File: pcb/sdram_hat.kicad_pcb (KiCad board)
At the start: 2 copper layers, 25 parts, among them J1 CONN_02X20, J2 CONN_02X20, J3 CONN_02X20, J4 CONN_02X20, J5 JACK_2P

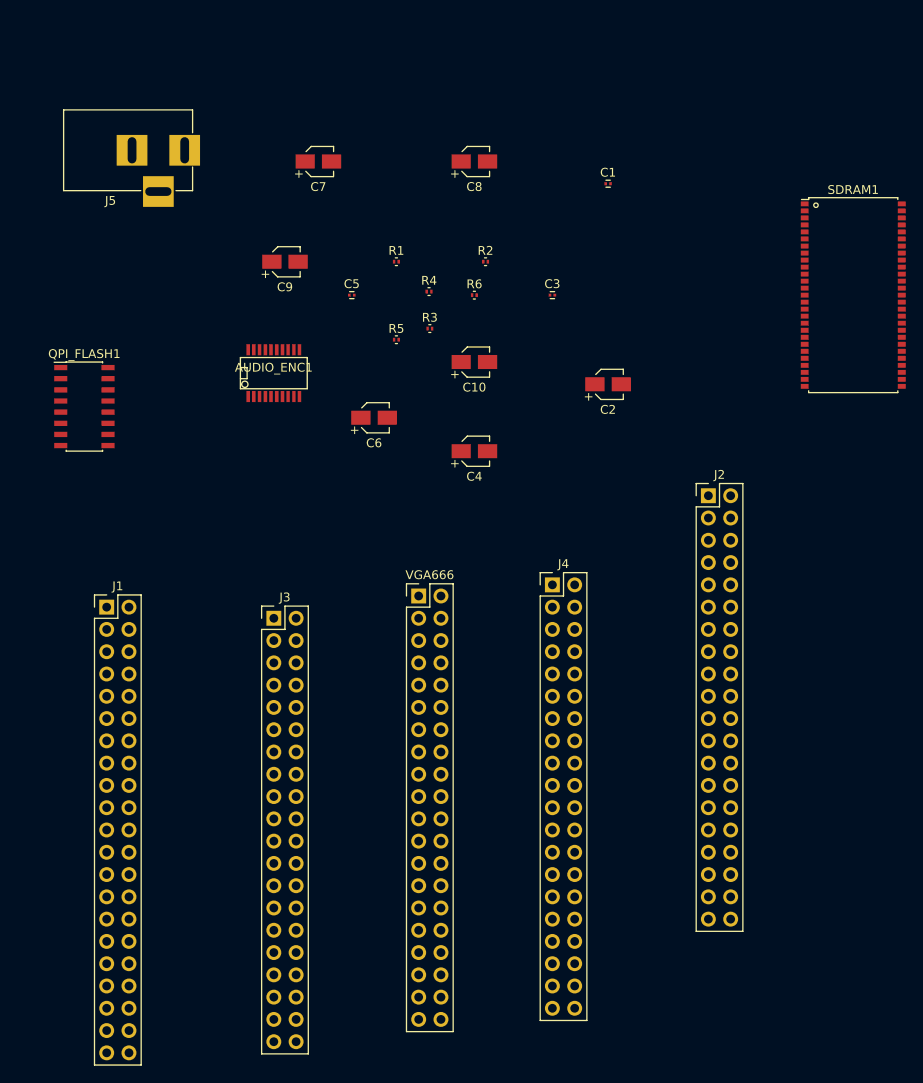
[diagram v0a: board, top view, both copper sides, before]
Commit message: Some additional layout work on PCB
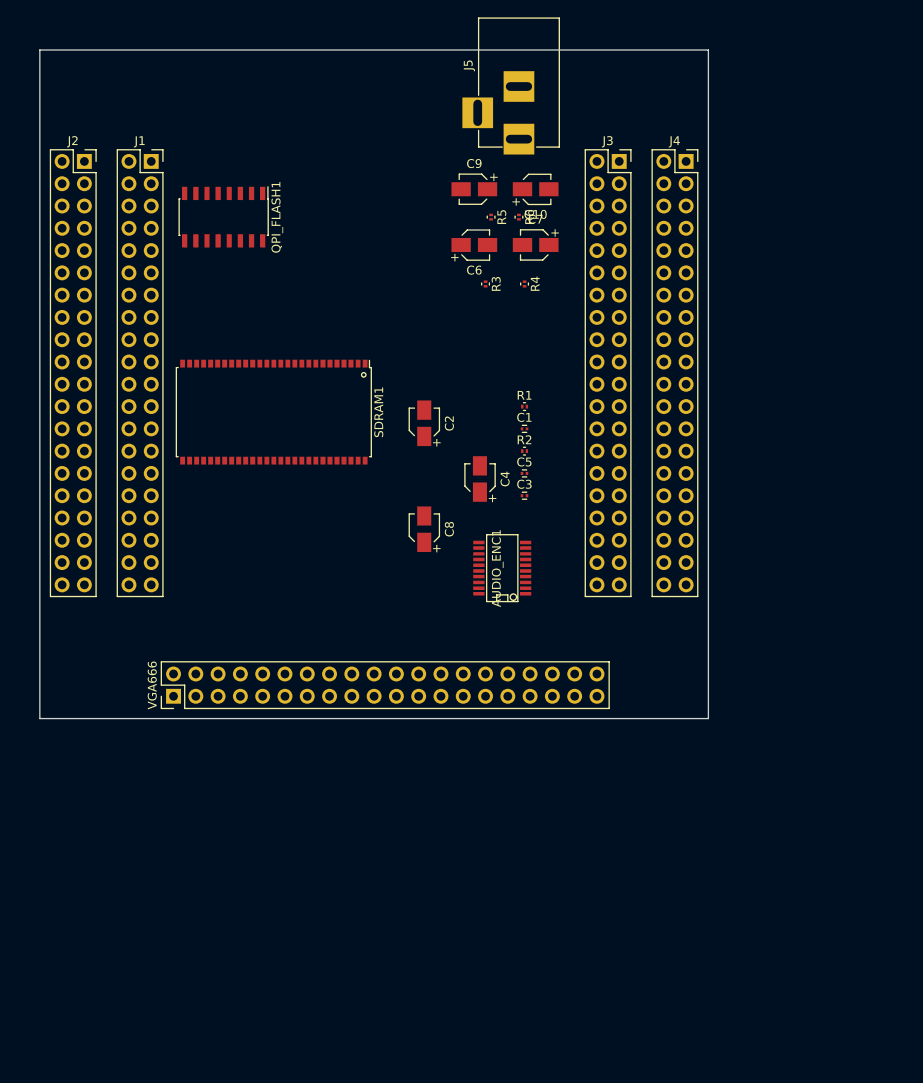
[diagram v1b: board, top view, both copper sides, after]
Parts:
- J1: footprint Pin_Headers:Pin_Header_Straight_2x21_Pitch2.54mm -> Socket_Strips:Socket_Strip_Straight_2x20_Pitch2.54mm
- J2, J3, J4: footprint Pin_Headers:Pin_Header_Straight_2x20_Pitch2.54mm -> Socket_Strips:Socket_Strip_Straight_2x20_Pitch2.54mm
- moved J2 80.7 mm to (20.3, 27.9)
- moved SDRAM1 67.4 mm to (41.9, 56.5), turned to 270 degrees
- moved J3 65.3 mm to (81.3, 27.9)
- moved J1 51.1 mm to (27.9, 27.9)
- moved J4 50.6 mm to (88.9, 27.9)
- moved C8 42.3 mm to (59.1, 69.8), turned to 90 degrees
- moved J5 38.1 mm to (69.8, 25.4), turned to 270 degrees
- moved AUDIO_ENC1 34.2 mm to (67.9, 74.3), turned to 90 degrees
- moved VGA666 30.2 mm to (30.5, 88.9), turned to 90 degrees
- moved C1 29.5 mm to (70.5, 58.4)
- moved C5 28.3 mm to (70.5, 63.5)
- moved QPI_FLASH1 26.8 mm to (36.2, 34.3), turned to 270 degrees
- moved C7 26.5 mm to (71.8, 37.5), turned to 180 degrees
- moved C9 23.1 mm to (64.8, 31.1), turned to 180 degrees
- moved C3 23.1 mm to (70.5, 66.0)
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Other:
- board outline added: 76.2 x 76.2 mm

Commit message: Added more pin definitions and progress on board layout
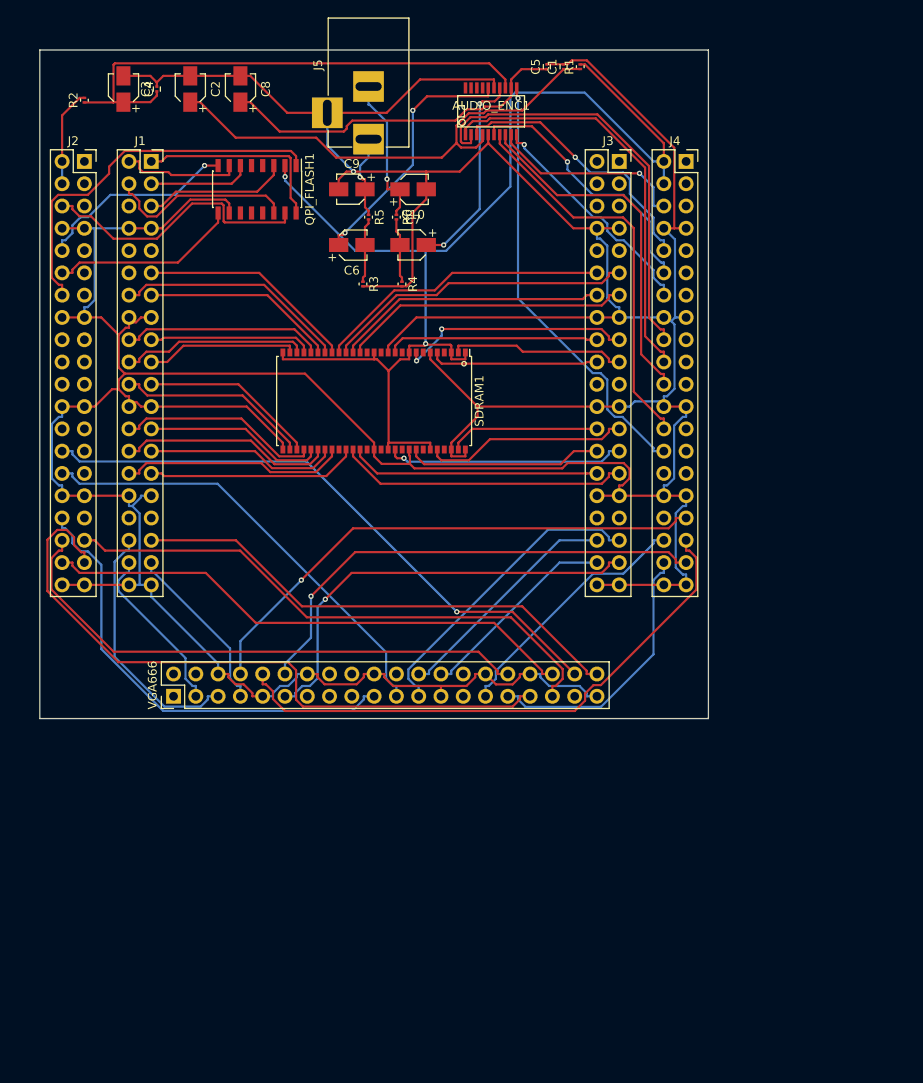
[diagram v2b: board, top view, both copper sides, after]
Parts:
- moved R2 64.2 mm to (20.3, 21.0), turned to 90 degrees
- moved C3 62.5 mm to (28.6, 19.7), turned to 90 degrees
- moved C4 60.2 mm to (24.8, 19.7)
- moved C8 54.4 mm to (38.1, 19.7)
- moved AUDIO_ENC1 52.1 mm to (66.7, 22.2), turned to 0 degrees
- moved C2 46.5 mm to (32.4, 19.7)
- moved C5 46.4 mm to (73.0, 17.1), turned to 90 degrees
- moved C1 41.5 mm to (74.9, 17.1), turned to 90 degrees
- moved R1 39.3 mm to (76.8, 17.1), turned to 90 degrees
- moved J5 17.1 mm to (52.7, 25.4)
- moved R3 14.0 mm to (52.1, 41.9)
- moved C10 14.0 mm to (57.8, 31.1)
- moved C6 14.0 mm to (50.8, 37.5)
- moved C7 14.0 mm to (57.8, 37.5)
- moved C9 14.0 mm to (50.8, 31.1)
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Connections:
- AUDIO_ENC1 pad 1: T16 -> DAC_BCK
- AUDIO_ENC1 pad 10: P13 -> DAC_PLL0
- AUDIO_ENC1 pad 11: R10 -> DAC_SFOR0
- AUDIO_ENC1 pad 2: T14 -> DAC_WS
- AUDIO_ENC1 pad 3: P10 -> DAC_DATAI
- AUDIO_ENC1 pad 6: M11 -> DAC_SYSCLK
- AUDIO_ENC1 pad 7: P9 -> DAC_SFOR1
- AUDIO_ENC1 pad 8: R9 -> DAC_MUTE
- AUDIO_ENC1 pad 9: T8 -> DAC_CLKOUT
- J1 pad 1: A16 -> IO0
- J1 pad 10: B11 -> B12
- J1 pad 11: A11 -> B10
- J1 pad 12: B10 -> A11
- J1 pad 13: A10 -> C9
- J1 pad 14: C9 -> A10
- J1 pad 17: A9 -> B9
- J1 pad 18: B9 -> A9
- J1 pad 19: B8 -> A7
- J1 pad 2: IO0 -> A16
- J1 pad 20: A7 -> B8
- J1 pad 21: B7 -> C7
- J1 pad 22: C7 -> B7
- J1 pad 25: A6 -> C6
- J1 pad 26: C6 -> A6
- J1 pad 27: B6 -> C5
- J1 pad 28: C5 -> B6
- J1 pad 29: A5 -> C4
- J1 pad 3: A15 -> B15
- J1 pad 30: C4 -> A5
- J1 pad 33: B5 -> C3
- J1 pad 34: C3 -> B5
- J1 pad 35: B4 -> B3
- J1 pad 36: B3 -> B4
- J1 pad 37: A2 -> A1
- J1 pad 38: A1 -> A2
- J1 pad 4: B15 -> A15
- J1 pad 5: B13 -> B14
- J1 pad 6: B14 -> B13
- J1 pad 9: B12 -> B11
- J2 pad 1: +1V2 -> IO1
- J2 pad 10: M15 -> N16
- J2 pad 11: M16 -> L16
- J2 pad 12: L16 -> M16
- J2 pad 13: K15 -> K16
- J2 pad 14: K16 -> K15
- J2 pad 17: K14 -> J14
- J2 pad 18: J14 -> K14
- J2 pad 19: G14 -> F14
- J2 pad 2: IO1 -> +1V2
- J2 pad 20: F14 -> G14
- J2 pad 21: J15 -> H14
- J2 pad 22: H14 -> J15
- J2 pad 25: H16 -> G15
- J2 pad 26: G15 -> H16
- J2 pad 27: G16 -> F15
- J2 pad 28: F15 -> G16
- J2 pad 29: F16 -> E14
- J2 pad 3: +1V2 -> R15
- J2 pad 30: E14 -> F16
- J2 pad 33: E16 -> D15
- J2 pad 34: D15 -> E16
- J2 pad 35: D16 -> D14
- J2 pad 36: D14 -> D16
- J2 pad 37: C16 -> B16
- J2 pad 38: B16 -> C16
- J2 pad 4: R15 -> +1V2
- J2 pad 5: P16 -> P15
- J2 pad 6: P15 -> P16
- J2 pad 9: N16 -> M15
- J3 pad 1: R16 -> IO2
- J3 pad 10: P13 -> N12
- J3 pad 11: N10 -> M11
- J3 pad 12: M11 -> N10
- J3 pad 13: T11 -> P10
- J3 pad 14: P10 -> SDRAM_CAS
- J3 pad 17: T10 -> R10
- J3 pad 18: R10 -> SDRAM_D3
- J3 pad 19: P8 -> P9
- J3 pad 2: IO2 -> R16
- J3 pad 20: P9 -> P8
- J3 pad 21: T9 -> R9
- J3 pad 22: R9 -> T9
- J3 pad 25: T7 -> SDRAM_D6
- J3 pad 26: T8 -> SDRAM_D7
- J3 pad 27: T6 -> R6
- J3 pad 28: R6 -> SDRAM_D5
- J3 pad 29: T5 -> R5
- J3 pad 3: T15 -> T16
- J3 pad 30: R5 -> SDRAM_DM
- J3 pad 33: R3 -> R4
- J3 pad 34: R4 -> R3
- J3 pad 35: R2 -> T3
- J3 pad 36: T3 -> R2
- J3 pad 37: T1 -> T2
- J3 pad 38: T2 -> T1
- J3 pad 4: T16 -> T15
- J3 pad 5: T13 -> T14
- J3 pad 6: T14 -> T13
- J3 pad 9: N12 -> P13
- J4 pad 1: +3V3 -> IO3
- J4 pad 10: N2 -> DAC_DATAI
- J4 pad 11: M2 -> M1
- J4 pad 12: M1 -> DAC_SYSCLK
- J4 pad 13: L3 -> L1
- J4 pad 14: L1 -> DAC_PLL0
- J4 pad 17: K3 -> K1
- J4 pad 18: K1 -> DAC_WS
- J4 pad 19: J2 -> J1
- J4 pad 2: IO3 -> +3V3
- J4 pad 20: J1 -> DAC_BCK
- J4 pad 21: H2 -> J3
- J4 pad 22: J3 -> DAC_MUTE
- J4 pad 25: G2 -> H1
- J4 pad 26: H1 -> DAC_SFOR1
- J4 pad 27: F2 -> G1
- J4 pad 28: G1 -> DAC_SFOR0
- J4 pad 29: E2 -> F1
- J4 pad 3: +3V3 -> R1
- J4 pad 30: F1 -> E2
- J4 pad 33: D1 -> D2
- J4 pad 34: D2 -> D1
- J4 pad 35: C1 -> C2
- J4 pad 36: C2 -> C1
- J4 pad 37: B1 -> B2
- J4 pad 38: B2 -> B1
- J4 pad 4: R1 -> +3V3
- J4 pad 5: P1 -> P2
- J4 pad 6: P2 -> DAC_CLKOUT
- J4 pad 9: N3 -> N2
- QPI_FLASH1 pad 1: T9 -> K15
- QPI_FLASH1 pad 14: N12 -> A15
- QPI_FLASH1 pad 15: T11 -> P16
- QPI_FLASH1 pad 16: T13 -> IO0
- QPI_FLASH1 pad 3: R16 -> B14
- QPI_FLASH1 pad 6: T15 -> B15
- QPI_FLASH1 pad 7: N10 -> A16
- QPI_FLASH1 pad 8: T10 -> N16
- QPI_FLASH1 pad 9: P8 -> M16
- SDRAM1 pad 11: F15 -> SDRAM_D3
- SDRAM1 pad 16: K16 -> P10
- SDRAM1 pad 17: L16 -> SDRAM_CAS
- SDRAM1 pad 18: M15 -> M11
- SDRAM1 pad 19: J14 -> N10
- SDRAM1 pad 2: F14 -> P9
- SDRAM1 pad 20: A15 -> B10
- SDRAM1 pad 21: B13 -> A10
- SDRAM1 pad 22: E16 -> C9
- SDRAM1 pad 23: P16 -> A9
- SDRAM1 pad 24: N16 -> B9
- SDRAM1 pad 25: M16 -> B8
- SDRAM1 pad 26: K15 -> A7
- SDRAM1 pad 29: K14 -> B7
- SDRAM1 pad 30: G14 -> C7
- SDRAM1 pad 31: J15 -> A6
- SDRAM1 pad 32: H16 -> C6
- SDRAM1 pad 33: G16 -> B6
- SDRAM1 pad 34: F16 -> C5
- SDRAM1 pad 35: D16 -> A5
- SDRAM1 pad 37: P15 -> C4
- SDRAM1 pad 38: R15 -> R5
- SDRAM1 pad 39: A16 -> SDRAM_DM
- SDRAM1 pad 44: E14 -> R6
- SDRAM1 pad 47: D15 -> SDRAM_D5
- SDRAM1 pad 5: H14 -> P8
- SDRAM1 pad 50: D14 -> SDRAM_D6
- SDRAM1 pad 53: B16 -> SDRAM_D7
- SDRAM1 pad 8: G15 -> R10
- VGA666 pad 10: Net-(VGA666-Pad10) -> C2
- VGA666 pad 11: Net-(VGA666-Pad11) -> T2
- VGA666 pad 12: Net-(VGA666-Pad12) -> B2
- VGA666 pad 14: Net-(VGA666-Pad14) -> GND
- VGA666 pad 19: Net-(VGA666-Pad19) -> E16
- VGA666 pad 20: Net-(VGA666-Pad20) -> GND
- VGA666 pad 21: Net-(VGA666-Pad21) -> F16
- VGA666 pad 23: Net-(VGA666-Pad23) -> T3
- VGA666 pad 24: Net-(VGA666-Pad24) -> R2
- VGA666 pad 25: Net-(VGA666-Pad25) -> GND
- VGA666 pad 26: Net-(VGA666-Pad26) -> T1
- VGA666 pad 29: Net-(VGA666-Pad29) -> C1
- VGA666 pad 3: Net-(VGA666-Pad3) -> A2
- VGA666 pad 30: Net-(VGA666-Pad30) -> GND
- VGA666 pad 31: Net-(VGA666-Pad31) -> B1
- VGA666 pad 32: Net-(VGA666-Pad32) -> D16
- VGA666 pad 33: Net-(VGA666-Pad33) -> B16
- VGA666 pad 34: Net-(VGA666-Pad34) -> GND
- VGA666 pad 35: Net-(VGA666-Pad35) -> D14
- VGA666 pad 36: Net-(VGA666-Pad36) -> C16
- VGA666 pad 38: Net-(VGA666-Pad38) -> G16
- VGA666 pad 39: Net-(VGA666-Pad39) -> GND
- VGA666 pad 40: Net-(VGA666-Pad40) -> B3
- VGA666 pad 5: Net-(VGA666-Pad5) -> B4
- VGA666 pad 6: Net-(VGA666-Pad6) -> GND
- VGA666 pad 7: Net-(VGA666-Pad7) -> A1
- VGA666 pad 8: Net-(VGA666-Pad8) -> D2
- VGA666 pad 9: Net-(VGA666-Pad9) -> GND
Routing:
- net GND: track 0.00 -> 559.8 mm, vias 0 -> 1
- net +3V3: track 0.00 -> 135.4 mm, vias 0 -> 2
- net B16: track 0.00 -> 76.4 mm
- net G16: track 0.00 -> 69.2 mm, vias 0 -> 1
- net C2: track 0.00 -> 64.9 mm
- net D14: track 0.00 -> 64.4 mm
- net D16: track 0.00 -> 62.6 mm
- net C16: track 0.00 -> 61.6 mm
- net D2: track 0.00 -> 60.6 mm, vias 0 -> 1
- net Net-(AUDIO_ENC1-Pad13): track 0.00 -> 59.8 mm
- net B3: track 0.00 -> 57.3 mm
- net Net-(AUDIO_ENC1-Pad4): track 0.00 -> 56.6 mm
- net B2: track 0.00 -> 55.6 mm, vias 0 -> 1
- net E16: track 0.00 -> 52.4 mm
- net F16: track 0.00 -> 51.3 mm
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
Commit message: Added TH passives, analog+digital ground planes, some autorouting stuff.
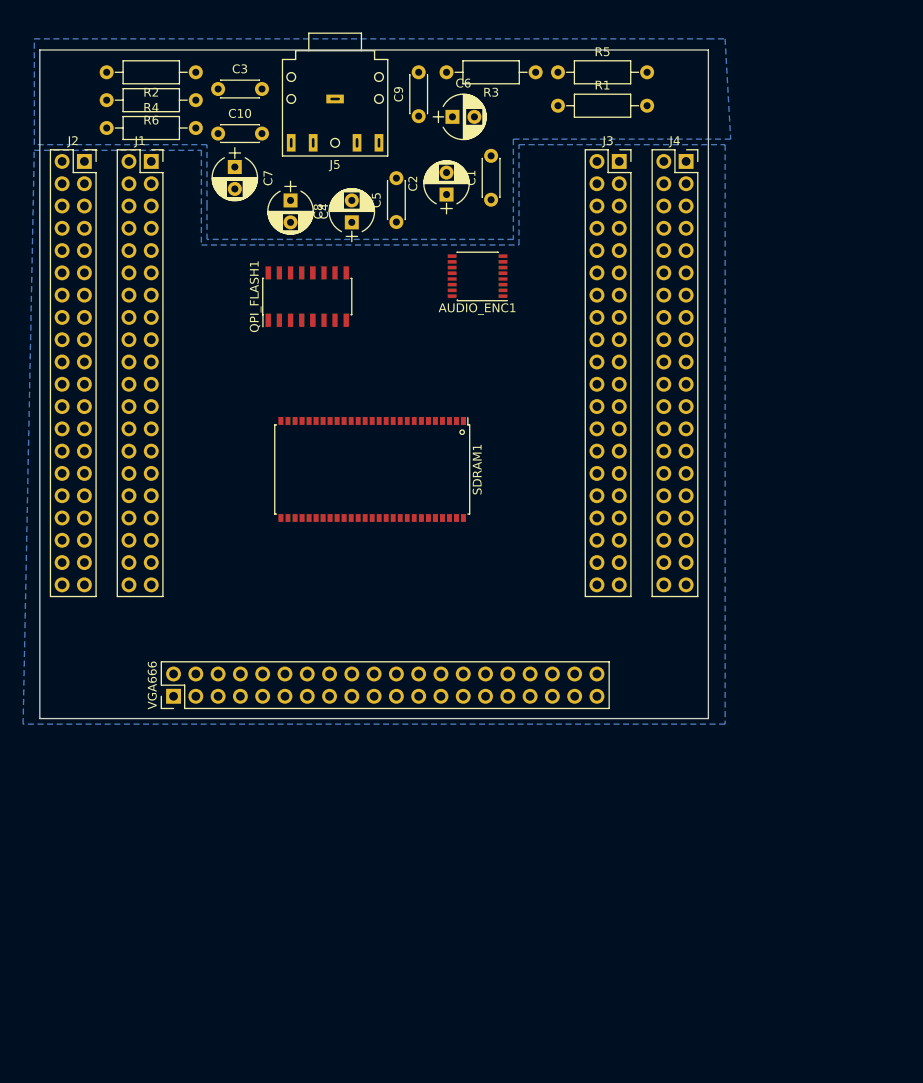
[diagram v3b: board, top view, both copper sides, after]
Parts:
- AUDIO_ENC1: footprint SMD_Packages:SSOP-20 -> Housings_SSOP:SSOP-16_4.4x5.2mm_Pitch0.65mm
- C1, C3, C5: footprint Capacitors_SMD:C_0201 -> Capacitors_THT:C_Disc_D4.3mm_W1.9mm_P5.00mm
- C10, C9: value 10nF 63V -> 10nF; footprint Capacitors_SMD:CP_Elec_3x5.3 -> Capacitors_THT:C_Disc_D4.3mm_W1.9mm_P5.00mm
- C2, C4, C6, C7, C8: footprint Capacitors_SMD:CP_Elec_3x5.3 -> Capacitors_THT:CP_Radial_D5.0mm_P2.50mm
- J5: value JACK_2P -> AUDIO_OUT_JACK; footprint Connectors:BARREL_JACK -> pcb:SJ1-352XNG
- R1, R2, R3, R4, R5, R6: footprint Resistors_SMD:R_0201 -> Resistors_THT:R_Axial_DIN0207_L6.3mm_D2.5mm_P10.16mm_Horizontal
- moved R4 38.1 mm to (22.9, 24.1), turned to 0 degrees
- moved C2 31.6 mm to (61.6, 31.7)
- moved R3 31.1 mm to (71.8, 17.8), turned to 180 degrees
- moved R5 27.2 mm to (74.3, 17.8), turned to 0 degrees
- moved R6 26.5 mm to (33.0, 21.0), turned to 180 degrees
- moved C5 24.6 mm to (55.9, 34.8)
- moved C10 23.1 mm to (35.6, 24.8)
- moved C4 22.9 mm to (43.8, 32.4), turned to 270 degrees
- moved C7 22.2 mm to (37.5, 28.6), turned to 270 degrees
- moved C8 19.8 mm to (50.8, 34.9)
- moved AUDIO_ENC1 18.8 mm to (65.1, 41.0), turned to 180 degrees
- moved C6 18.6 mm to (62.3, 22.9)
- moved C1 17.3 mm to (66.7, 32.3)
- moved QPI_FLASH1 13.5 mm to (45.7, 43.3), turned to 90 degrees
- moved R2 13.1 mm to (33.0, 17.8), turned to 180 degrees
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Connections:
- AUDIO_ENC1 pad 15: GND -> GNDA
- AUDIO_ENC1 pad 5: GND -> GNDA
- C1 pad 2: GND -> GNDA
- C2 pad 2: GND -> GNDA
- C3 pad 2: GND -> GNDA
- C4 pad 2: GND -> GNDA
- C5 pad 2: GND -> GNDA
- C8 pad 2: GND -> GNDA
- J1 pad 1: IO0 -> (no net)
- J1 pad 11: B10 -> (no net)
- J1 pad 12: A11 -> (no net)
- J1 pad 14: A10 -> (no net)
- J1 pad 18: A9 -> (no net)
- J1 pad 2: A16 -> (no net)
- J1 pad 20: B8 -> (no net)
- J1 pad 33: C3 -> (no net)
- J1 pad 34: B5 -> (no net)
- J1 pad 37: A1 -> (no net)
- J1 pad 4: A15 -> (no net)
- J2 pad 1: IO1 -> (no net)
- J2 pad 10: N16 -> (no net)
- J2 pad 11: L16 -> (no net)
- J2 pad 13: K16 -> (no net)
- J2 pad 17: J14 -> (no net)
- J2 pad 18: K14 -> (no net)
- J2 pad 20: G14 -> (no net)
- J2 pad 22: J15 -> (no net)
- J2 pad 26: H16 -> (no net)
- J2 pad 28: G16 -> (no net)
- J2 pad 29: E14 -> (no net)
- J2 pad 3: R15 -> (no net)
- J2 pad 30: F16 -> (no net)
- J2 pad 6: P16 -> (no net)
- J3 pad 1: IO2 -> DAC_PLL0
- J3 pad 10: N12 -> (no net)
- J3 pad 2: R16 -> DAC_CLKOUT
- J3 pad 21: R9 -> (no net)
- J3 pad 22: T9 -> (no net)
- J3 pad 3: T16 -> DAC_WS
- J3 pad 33: R4 -> (no net)
- J3 pad 34: R3 -> (no net)
- J3 pad 4: T15 -> DAC_DATAI
- J3 pad 5: T14 -> DAC_BCK
- J3 pad 6: T13 -> DAC_SFOR1
- J3 pad 9: P13 -> (no net)
- J4 pad 1: IO3 -> (no net)
- J4 pad 10: DAC_DATAI -> DAC_SFOR0
- J4 pad 11: M1 -> (no net)
- J4 pad 13: L1 -> (no net)
- J4 pad 14: DAC_PLL0 -> (no net)
- J4 pad 17: K1 -> (no net)
- J4 pad 18: DAC_WS -> (no net)
- J4 pad 19: J1 -> (no net)
- J4 pad 20: DAC_BCK -> (no net)
- J4 pad 21: J3 -> (no net)
- J4 pad 22: DAC_MUTE -> (no net)
- J4 pad 25: H1 -> (no net)
- J4 pad 26: DAC_SFOR1 -> (no net)
- J4 pad 28: DAC_SFOR0 -> (no net)
- J4 pad 3: R1 -> (no net)
- J4 pad 30: E2 -> (no net)
- J4 pad 34: D1 -> (no net)
- J4 pad 5: P2 -> (no net)
- J4 pad 6: DAC_CLKOUT -> DAC_MUTE
- J4 pad 9: N2 -> (no net)
- J5 pad 1: Net-(C9-Pad1) -> GNDA
- J5 pad 3: GND -> Net-(C9-Pad1)
- QPI_FLASH1 pad 1: K15 -> M15
- QPI_FLASH1 pad 14: A15 -> B12
- QPI_FLASH1 pad 15: P16 -> M16
- QPI_FLASH1 pad 16: IO0 -> B15
- QPI_FLASH1 pad 3: B14 -> B11
- QPI_FLASH1 pad 6: B15 -> B14
- QPI_FLASH1 pad 7: A16 -> B13
- QPI_FLASH1 pad 8: N16 -> K15
- QPI_FLASH1 pad 9: M16 -> P15
- SDRAM1 pad 20: B10 -> B9
- SDRAM1 pad 21: A10 -> C9
- SDRAM1 pad 22: C9 -> A7
- SDRAM1 pad 23: A9 -> F14
- SDRAM1 pad 24: B9 -> H14
- SDRAM1 pad 25: B8 -> G15
- SDRAM1 pad 26: A7 -> F15
- VGA666 pad 1: Net-(VGA666-Pad1) -> (no net)
- VGA666 pad 10: C2 -> B16
- VGA666 pad 11: T2 -> D15
- VGA666 pad 12: B2 -> B4
- VGA666 pad 13: Net-(VGA666-Pad13) -> (no net)
- VGA666 pad 15: Net-(VGA666-Pad15) -> (no net)
- VGA666 pad 16: Net-(VGA666-Pad16) -> (no net)
- VGA666 pad 17: Net-(VGA666-Pad17) -> (no net)
- VGA666 pad 18: Net-(VGA666-Pad18) -> (no net)
- VGA666 pad 19: E16 -> A2
- VGA666 pad 2: Net-(VGA666-Pad2) -> (no net)
- VGA666 pad 21: F16 -> B3
- VGA666 pad 22: Net-(VGA666-Pad22) -> (no net)
- VGA666 pad 23: T3 -> B2
- VGA666 pad 27: Net-(VGA666-Pad27) -> (no net)
- VGA666 pad 28: Net-(VGA666-Pad28) -> (no net)
- VGA666 pad 29: C1 -> G1
- VGA666 pad 3: A2 -> D16
- VGA666 pad 31: B1 -> F1
- VGA666 pad 32: D16 -> T3
- VGA666 pad 33: B16 -> C2
- VGA666 pad 35: D14 -> D2
- VGA666 pad 36: C16 -> T2
- VGA666 pad 37: Net-(VGA666-Pad37) -> (no net)
- VGA666 pad 38: G16 -> C1
- VGA666 pad 4: Net-(VGA666-Pad4) -> (no net)
- VGA666 pad 40: B3 -> B1
- VGA666 pad 5: B4 -> C16
- VGA666 pad 7: A1 -> E16
- VGA666 pad 8: D2 -> D14
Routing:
- net GND: track 559.8 -> 0.00 mm, vias 1 -> 0
- net +3V3: track 135.4 -> 0.00 mm, vias 2 -> 0
- net B16: track 76.4 -> 0.00 mm
- net G16: track 69.2 -> 0.00 mm, vias 1 -> 0
- net C2: track 64.9 -> 0.00 mm
- net D14: track 64.4 -> 0.00 mm
- net D16: track 62.6 -> 0.00 mm
- net C16: track 61.6 -> 0.00 mm
- net D2: track 60.6 -> 0.00 mm, vias 1 -> 0
- net Net-(AUDIO_ENC1-Pad13): track 59.8 -> 0.00 mm
- net B3: track 57.3 -> 0.00 mm
- net Net-(AUDIO_ENC1-Pad4): track 56.6 -> 0.00 mm
- net B2: track 55.6 -> 0.00 mm, vias 1 -> 0
- net E16: track 52.4 -> 0.00 mm
- net F16: track 51.3 -> 0.00 mm
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- added copper zone on B.Cu, net GND
- added copper zone on B.Cu, net GNDA
